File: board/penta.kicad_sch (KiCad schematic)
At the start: 162 parts, among them J1 USB_C_Receptacle, U1 MIC5504-3.3YM5, U2 RP2040, U3 W25Q32JVSS, Y1 12000Hz

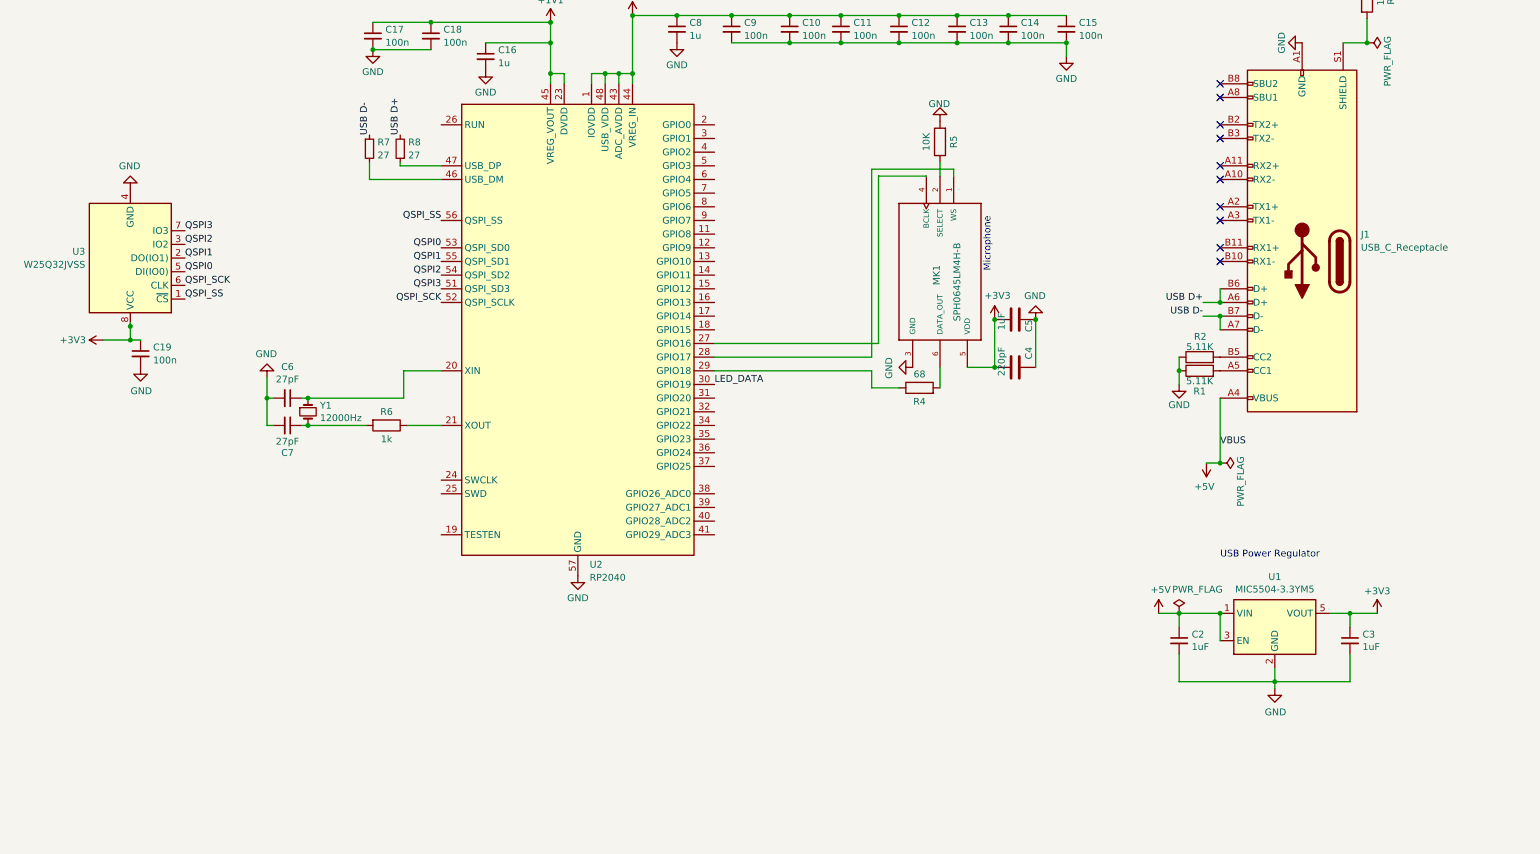
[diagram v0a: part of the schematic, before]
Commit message: schematic for a boost chip that we may not actually need; + wc changes
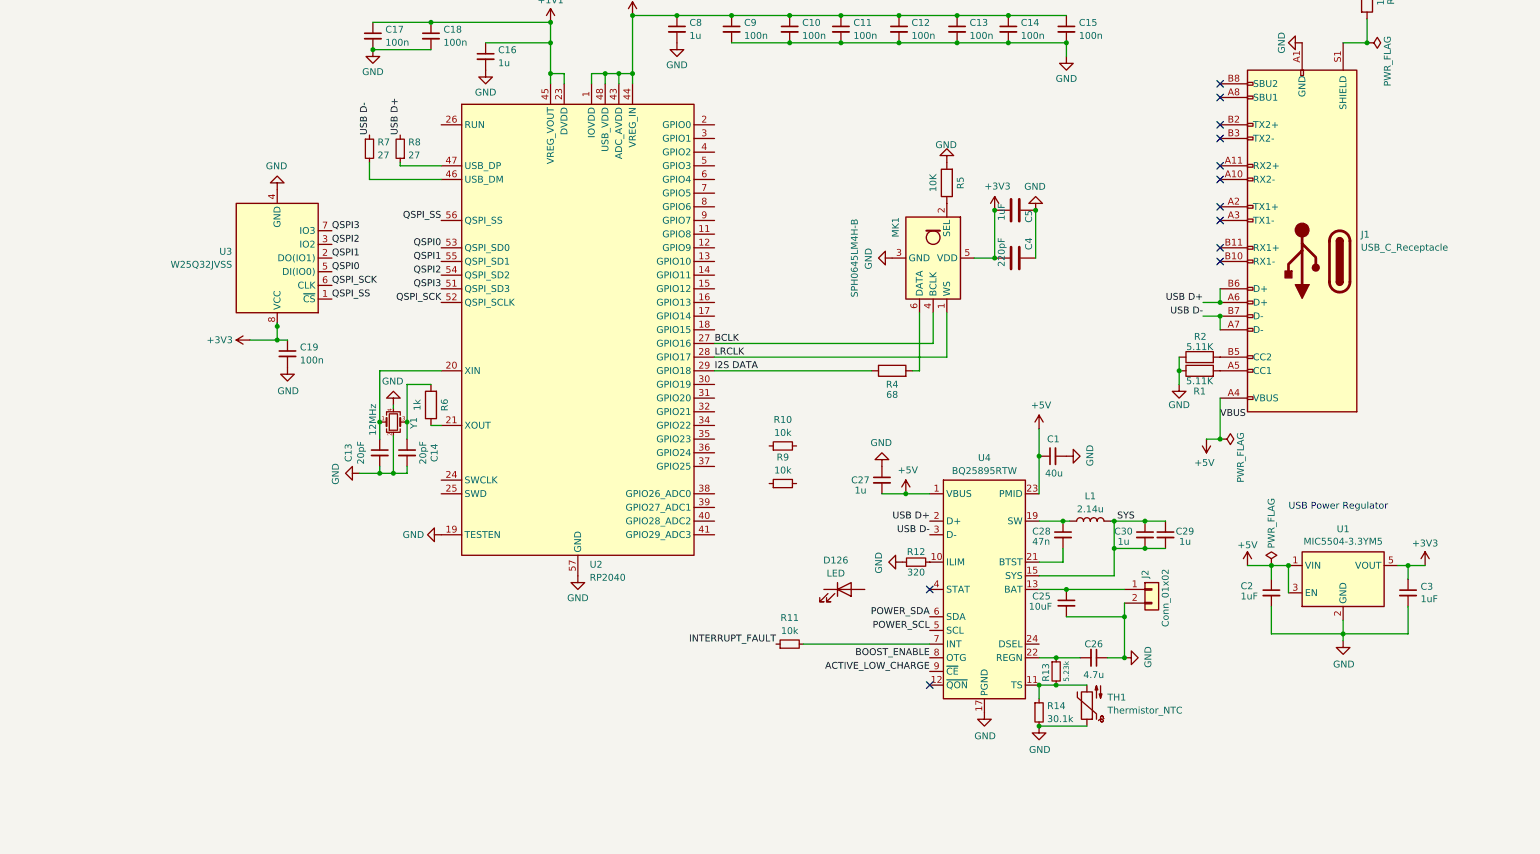
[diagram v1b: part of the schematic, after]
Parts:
- removed C6, C7: 27pF, Capacitor_SMD:C_0402_1005Metric, symbol Device:C_Small
- removed Y1: 12000Hz, Crystal:Crystal_SMD_3215-2Pin_3.2x1.5mm, symbol Device:Crystal_Small
- added C1: 40u, Capacitor_SMD:C_0201_0603Metric, symbol Device:C_Small
- added C13, C14: 20pF, Capacitor_SMD:C_0402_1005Metric, symbol Device:C_Small
- added C25: 10uF, Capacitor_SMD:C_0402_1005Metric, symbol Device:C_Small
- added C26: 4.7u, symbol Device:C_Small
- added C27, C29, C30: 1u, Capacitor_SMD:C_0402_1005Metric, symbol Device:C_Small
- added C28: 47n, Capacitor_SMD:C_0402_1005Metric, symbol Device:C_Small
- added D126: LED, symbol Device:LED
- added J2: Conn_01x02, Connector_JST:JST_PH_S2B-PH-SM4-TB_1x02-1MP_P2.00mm_Horizontal, symbol Connector_Generic:Conn_01x02
- added L1: 2.14u, symbol Device:L
- added R10, R11, R9: 10k, symbol Device:R_Small
- added R12: 320, symbol Device:R_Small
- added R13: 5.23k, symbol Device:R_Small
- added R14: 30.1k, symbol Device:R_Small
- added TH1: Thermistor_NTC, Resistor_SMD:R_0402_1005Metric, symbol Device:Thermistor_NTC
- added U4: BQ25895RTW, Package_DFN_QFN:Texas_S-PWQFN-N24_EP2.7x2.7mm_ThermalVias, symbol Battery_Management:BQ25895RTW
- added Y1: 12MHz, Crystal:Crystal_SMD_3225-4Pin_3.2x2.5mm, symbol Device:Crystal_GND24_Small
- MK1: footprint penta:MIC_SPH0645LM4H-B -> Sensor_Audio:Knowles_SPH0645LM4H-6_3.5x2.65mm; symbol earthvenusmars:SPH0645LM4H-B-Mic_I2S -> Sensor_Audio:SPH0645LM4H
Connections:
- net +5V: now also C1.1, C27.2, U4.1 (VBUS), U4.23 (PMID)
- net GND: now also U2.19 (TESTEN), C1.2, C13.2, C14.2, C25.2, C26.1, C27.1, J2.2 (Pin_2), R12.1, R14.2, TH1.1, U4.17 (PGND), U4.18 (PGND), U4.25 (PGND), Y1.2, Y1.4
- net LED_DATA: no longer U2.30 (GPIO19)
- net USB D+: now also U4.2 (D+)
- net USB D-: now also U4.3 (D-)
- net at R6.2: now also C14.1, Y1.3
- net at U2.20 (XIN): now also C13.1, Y1.1
- net LRCLK: now reaches MK1.1 (WS), U2.28 (GPIO17)
- net BCLK: now reaches MK1.4 (BCLK), U2.27 (GPIO16)
- net I2S DATA: now reaches R4.1, U2.29 (GPIO18)
- new net: C28.1, L1.1, U4.19 (SW), U4.20 (SW)
- new net: R12.2, U4.10 (ILIM)
- new net: R11.2, U4.7 (INT)
- new net: C25.1, J2.1 (Pin_1), U4.13 (BAT), U4.14 (BAT)
- new net: R13.2, R14.1, TH1.2, U4.11 (TS)
- new net: C28.2, U4.21 (BTST)
- new net: C26.2, R13.1, U4.22 (REGN)
- new net ACTIVE_LOW_CHARGE: U4.9 (~{CE})
- new net BOOST_ENABLE: U4.8 (OTG)
- new net INTERRUPT_FAULT: R11.1
- new net POWER_SCL: U4.5 (SCL)
- new net POWER_SDA: U4.6 (SDA)
- new net SYS: C29.1, C29.2, C30.1, C30.2, L1.2, U4.15 (SYS), U4.16 (SYS)
- no-connect marks 11 -> 13
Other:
- note removed: "Microphone"
- moved on the sheet: C19, C2, C3, C4, C5, R4, R5, R6, U1, U3

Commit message: completely rework everything but the pixels; base it off seeeduino for ease/cost; add a usb port for chaining; add a microphone
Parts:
- removed C1: 40u, Capacitor_SMD:C_0201_0603Metric, symbol Device:C_Small
- removed C10, C11, C12, C13, C14, C15, C17, C18, C19, C9: 100n, Capacitor_SMD:C_0402_1005Metric, symbol Device:C_Small
- removed C13, C14: 20pF, Capacitor_SMD:C_0402_1005Metric, symbol Device:C_Small
- removed C16, C27, C29, C30, C8: 1u, Capacitor_SMD:C_0402_1005Metric, symbol Device:C_Small
- removed C2, C3: 1uF, Capacitor_SMD:C_0402_1005Metric, symbol Device:C_Small
- removed C25: 10uF, Capacitor_SMD:C_0402_1005Metric, symbol Device:C_Small
- removed C26: 4.7u, symbol Device:C_Small
- removed C28: 47n, Capacitor_SMD:C_0402_1005Metric, symbol Device:C_Small
- removed C4: 220pF, Capacitor_SMD:C_0402_1005Metric, symbol Device:C
- removed C5: 1uF, Capacitor_SMD:C_0402_1005Metric, symbol Device:C
- removed D126: LED, symbol Device:LED
- removed J1: USB_C_Receptacle, Connector_USB:USB_C_Receptacle_GCT_USB4110, symbol Connector:USB_C_Receptacle
- removed J2: Conn_01x02, Connector_JST:JST_PH_S2B-PH-SM4-TB_1x02-1MP_P2.00mm_Horizontal, symbol Connector_Generic:Conn_01x02
- removed L1: 2.14u, symbol Device:L
- removed MK1: SPH0645LM4H-B, Sensor_Audio:Knowles_SPH0645LM4H-6_3.5x2.65mm, symbol Sensor_Audio:SPH0645LM4H
- removed R10, R11, R9: 10k, symbol Device:R_Small
- removed R12: 320, symbol Device:R_Small
- removed R13: 5.23k, symbol Device:R_Small
- removed R14: 30.1k, symbol Device:R_Small
- removed R3: 1M, Resistor_SMD:R_0402_1005Metric, symbol Device:R
- removed R4: 68, Resistor_SMD:R_0402_1005Metric, symbol Device:R
- removed R5: 10K, Resistor_SMD:R_0402_1005Metric, symbol Device:R
- removed R6: 1k, Resistor_SMD:R_0402_1005Metric, symbol Device:R
- removed R7, R8: 27, Resistor_SMD:R_0402_1005Metric, symbol Device:R_Small
- removed TH1: Thermistor_NTC, Resistor_SMD:R_0402_1005Metric, symbol Device:Thermistor_NTC
- removed U1: MIC5504-3.3YM5, Package_TO_SOT_SMD:SOT-23-5, symbol Regulator_Linear:MIC5504-3.3YM5
- removed U2: RP2040, Package_DFN_QFN:QFN-56-1EP_7x7mm_P0.4mm_EP3.2x3.2mm, symbol MCU_RaspberryPi:RP2040
- removed U3: W25Q32JVSS, Package_SO:SOIC-8_5.23x5.23mm_P1.27mm, symbol Memory_Flash:W25Q32JVSS
- removed U4: BQ25895RTW, Package_DFN_QFN:Texas_S-PWQFN-N24_EP2.7x2.7mm_ThermalVias, symbol Battery_Management:BQ25895RTW
- removed Y1: 12MHz, Crystal:Crystal_SMD_3225-4Pin_3.2x2.5mm, symbol Device:Crystal_GND24_Small
- added C1: 100nF, Capacitor_SMD:C_0402_1005Metric, symbol Device:C
- added J1: USB_C_Receptacle_PowerOnly_6P, penta:USB-C-SMD_TYPE-C-6P-QT073, symbol Connector:USB_C_Receptacle_PowerOnly_6P
- added MIC1: LMD4737T263-OY1, easyeda2kicad:LGA-6_L4.7-W3.8-P1.65_LMD4737T, symbol penta:LMD4737T263-OY1
- added U1: XIAO-RP2040-SMD, penta:XIAO-RP2040-SMD, symbol penta:XIAO-RP2040-SMD
- D1, D10, D100, D101, D102, D103, D104, D105, D106, D107, D108, D109, D11, D110, D111, D112, D113, D114, D115, D116, D117, D118, D119, D12, D120, D121, D122, D123, D124, D125, D13, D14, D15, D16, D17, D18, D19, D2, D20, D21, D22, D23, D24, D25, D26, D27, D28, D29, D3, D30, D31, D32, D33, D34, D35, D36, D37, D38, D39, D4, D40, D41, D42, D43, D44, D45, D46, D47, D48, D49, D5, D50, D51, D52, D53, D54, D55, D56, D57, D58, D59, D6, D60, D61, D62, D63, D64, D65, D66, D67, D68, D69, D7, D70, D71, D72, D73, D74, D75, D76, D77, D78, D79, D8, D80, D81, D82, D83, D84, D85, D86, D87, D88, D89, D9, D90, D91, D92, D93, D94, D95, D96, D97, D98, D99: Designation (none) -> XL-1010RGBC-WS2812B; LCSC (none) -> C5349953
- R1, R2: Designation (none) -> RC0402FR-07511KL; LCSC (none) -> C163461
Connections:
- net +3V3: now also C1.1, MIC1.6 (VDD), U1.12 (3V3)
- net +5V: now also J1.A9 (VBUS), J1.B9 (VBUS), U1.14 (5V)
- net BCLK: now also MIC1.4 (CLK), U1.9 (GPIO2_D8_SCK)
- net GND: now also R2.2, C1.2, J1.A12 (GND), J1.B12 (GND), J1.S1 (SHIELD), MIC1.1 (GND), MIC1.3 (GND), U1.13 (GND), U1.16 (GND), U1.20 (GND); no longer R2.1
- net I2S DATA: now also MIC1.5 (DATA), U1.10 (GPIO4_D9_MISO)
- net LED_DATA: now also U1.2 (GPIO27_A1_D1)
- net LRCLK: now also MIC1.2 (L/R), U1.11 (GPIO3_D10_MOSI)
- net at R1.2: now also J1.A5 (CC1)
- new net: J1.B5 (CC2), R2.1
- no-connect marks 13 -> 12
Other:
- note removed: "USB Power Regulator"
- moved on the sheet: C20, C21, C22, C23, C24, D1, D10, D100, D101, D102, D103, D104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

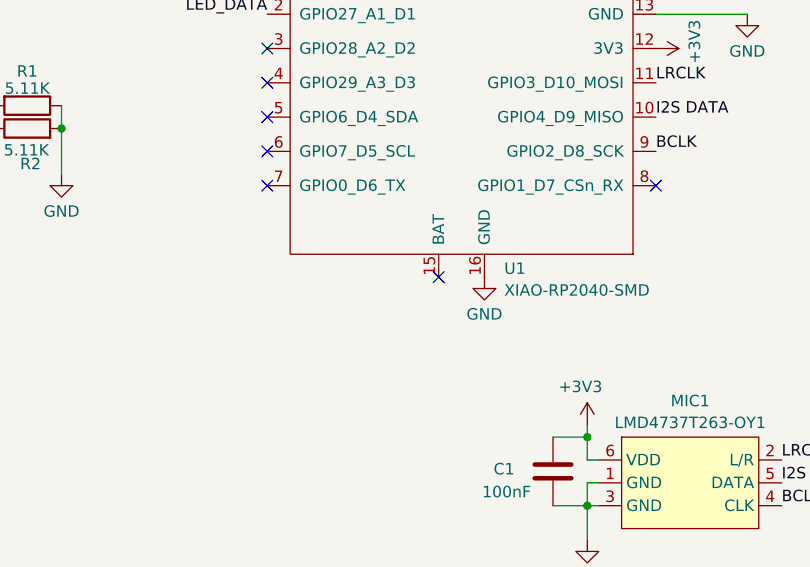
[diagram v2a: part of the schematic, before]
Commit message: myriad improvements. mounting points for idk, nice symmetric. removed unnecessary pads from seeduino footprint to make room for mount points; added exposed ldo VIN pin to seeduino footprint bc it's VBUS >| VIN so it can supply leds (and made those pins longer so they can be manually soldered and still; improved zone fills;
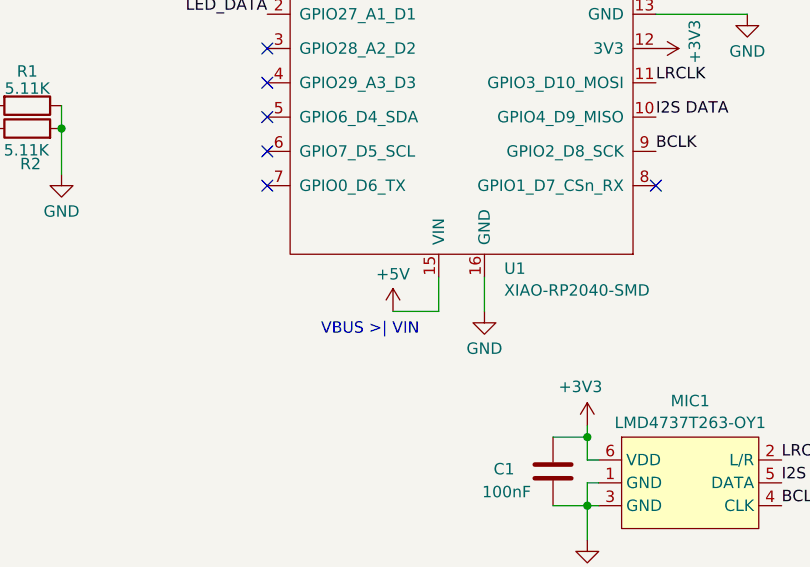
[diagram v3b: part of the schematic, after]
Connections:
- net +5V: now also U1.15 (VIN)
- no-connect marks 12 -> 11
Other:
- note added: "VBUS >| VIN"
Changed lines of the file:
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@@
 	)
 	(no_connect
-		(at 189.23 109.22)
-	)
-	(no_connect
 		(at 189.23 64.77)
 	)
@@
 	(wire
 		(pts
+			(xy 194.31 113.03) (xy 194.31 109.22)
+		)
+		(stroke
+			(width 0)
+			(type default)
+		)
+	)
+	(wire
+		(pts
 			(xy 458.47 179.07) (xy 473.71 179.07)
 		)
@@
 	(wire
 		(pts
+			(xy 189.23 109.22) (xy 189.23 113.03)
+		)
+		(stroke
+			(width 0)
+			(type default)
+		)
+	)
+	(wire
+		(pts
 			(xy 351.79 234.95) (xy 367.03 234.95)
 		)
@@
 	(wire
 		(pts
+			(xy 189.23 113.03) (xy 184.15 113.03)
+		)
+		(stroke
+			(width 0)
+			(type default)
+		)
+	)
+	(wire
+		(pts
 			(xy 336.55 90.17) (xy 351.79 90.17)
 		)
@@
 		)
 	)
+	(text "VBUS >| VIN"
+		(exclude_from_sim no)
+		(at 181.61 115.062 0)
+		(effects
+			(font
+				(size 1.27 1.27)
+			)
+		)
+	)
 	(label "LED_DATA"
 		(at 328.93 26.67 180)
@@
 	(symbol
 		(lib_id "power:GND")
-		(at 194.31 109.22 0)
+		(at 194.31 113.03 0)
 		(unit 1)
 		(exclude_from_sim no)
@@
 		(fields_autoplaced yes)
 		(property "Reference" "#PWR03"
-			(at 194.31 115.57 0)
+			(at 194.31 119.38 0)
 			(effects
 				(font
@@
 		)
 		(property "Value" "GND"
-			(at 194.31 113.3531 0)
+			(at 194.31 117.1631 0)
 			(effects
 				(font
@@
 		)
 		(property "Footprint" ""
-			(at 194.31 109.22 0)
+			(at 194.31 113.03 0)
 			(effects
 				(font
@@
 		)
 		(property "Datasheet" ""
-			(at 194.31 109.22 0)
+			(at 194.31 113.03 0)
 			(effects
 				(font
@@
 		)
 		(property "Description" "Power symbol creates a global label with name \"GND\" , ground"
-			(at 194.31 109.22 0)
+			(at 194.31 113.03 0)
 			(effects
 				(font
@@
 					(unit 1)
 				)
+			)
+		)
+	)
+	(symbol
+		(lib_id "power:+5V")
+		(at 184.15 113.03 0)
+		(unit 1)
+		(exclude_from_sim no)
+		(in_bom yes)
+		(on_board yes)
+		(dnp no)
+		(fields_autoplaced yes)
+		(property "Reference" "#PWR013"
+			(at 184.15 116.84 0)
+			(effects
+				(font
+					(size 1.27 1.27)
+				)
+				(hide yes)
+			)
+		)
+		(property "Value" "+5V"
+			(at 184.15 108.8969 0)
+			(effects
+				(font
+					(size 1.27 1.27)
+				)
+			)
+		)
+		(property "Footprint" ""
+			(at 184.15 113.03 0)
+			(effects
+				(font
+					(size 1.27 1.27)
+				)
+				(hide yes)
+			)
+		)
+		(property "Datasheet" ""
+			(at 184.15 113.03 0)
+			(effects
+				(font
+					(size 1.27 1.27)
+				)
+				(hide yes)
+			)
+		)
+		(property "Description" "Power symbol creates a global label with name \"+5V\""
+			(at 184.15 113.03 0)
+			(effects
+				(font
+					(size 1.27 1.27)
+				)
+				(hide yes)
+			)
+		)
+		(pin "1"
+		)
+		(instances
+			(project "penta"
+				(path "/2e8b15b9-33da-4001-b66c-591b57065bcb"
+					(reference "#PWR013")
+					(unit 1)
+				)

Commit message: add 3 gpios to the screwmounts, which are now thts. maybe these can be used for capacitive touch?
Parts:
- added TP1, TP2, TP3, TP4, TP5: TestPoint, penta:ScrewTouchHole, symbol Connector:TestPoint
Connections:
- net GND: no longer J1.S1 (SHIELD)
- net TOUCH1: now reaches U1.1 (GPIO26_A0_D0)
- net TOUCH1: now also TP1.1
- net TOUCH2: now reaches U1.5 (GPIO6_D4_SDA)
- net TOUCH2: now also TP2.1
- net TOUCH3: now reaches U1.8 (GPIO1_D7_CSn_RX)
- net TOUCH3: now also TP5.1
- new net: J1.S1 (SHIELD), TP3.1, TP4.1
- no-connect marks 11 -> 7
